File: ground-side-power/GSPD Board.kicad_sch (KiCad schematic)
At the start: 37 parts, among them J2 Battery Terminals, J4 Battery Terminals, J6 To SP2T, J7 From SP3T, J8 To On SW, J9 From Off SW, K1 AZ2150-1A-12DEF, U1 K7805-3AR3, U2 URB2424LD-20WR3

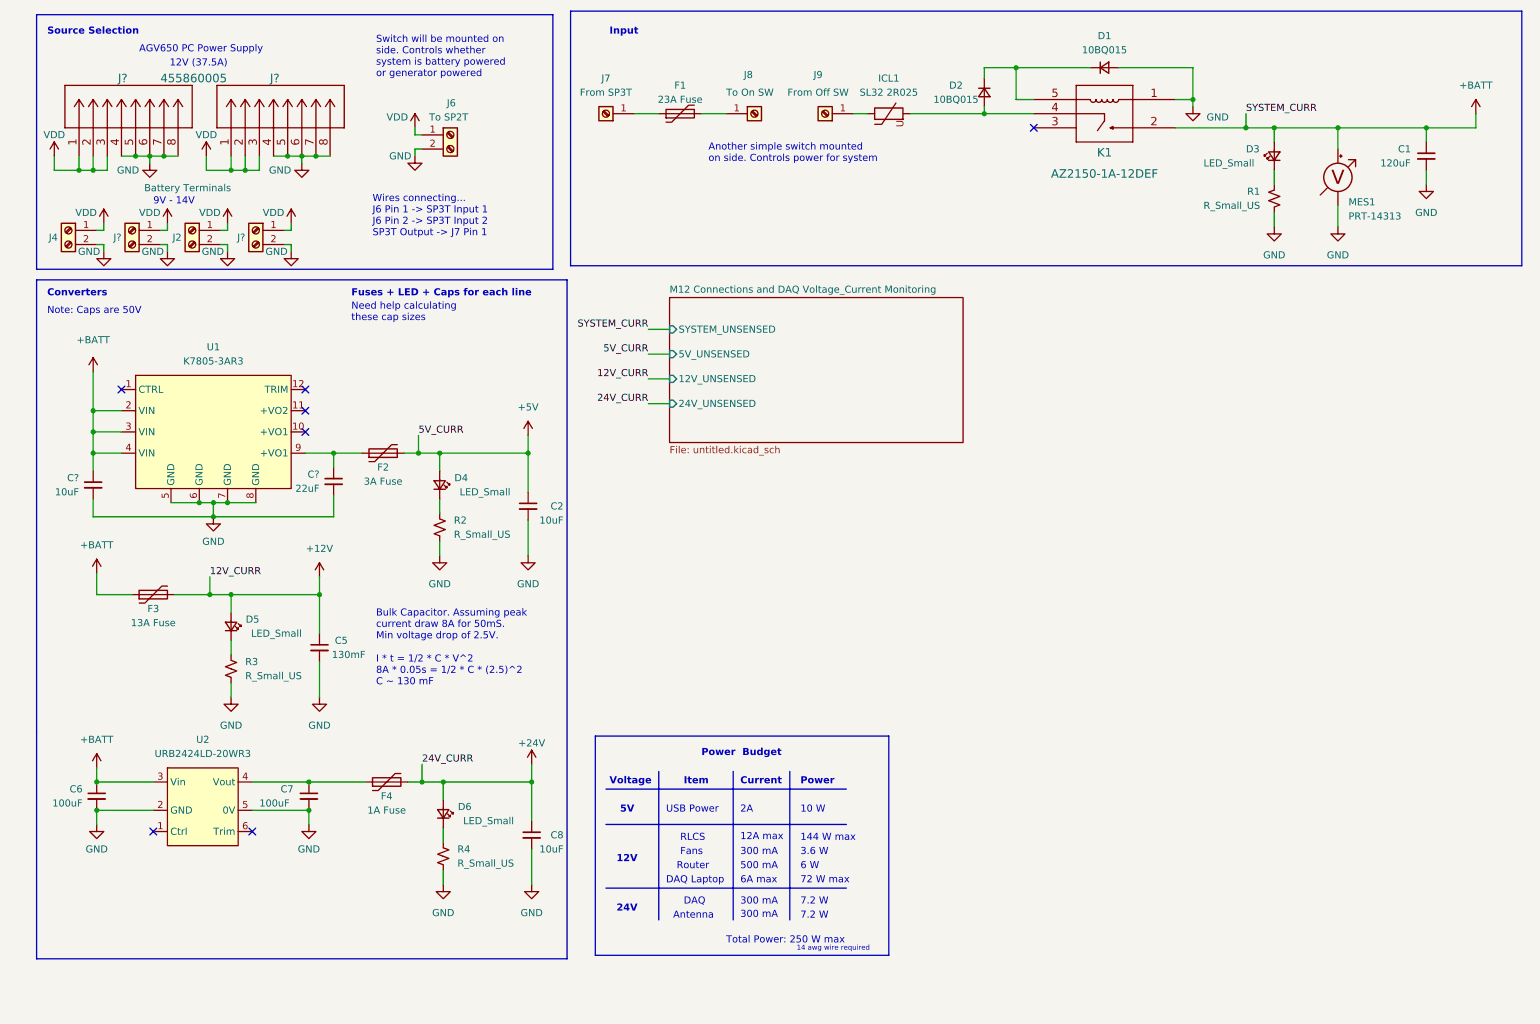
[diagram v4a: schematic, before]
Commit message: Changes to Shunt Current Sensors
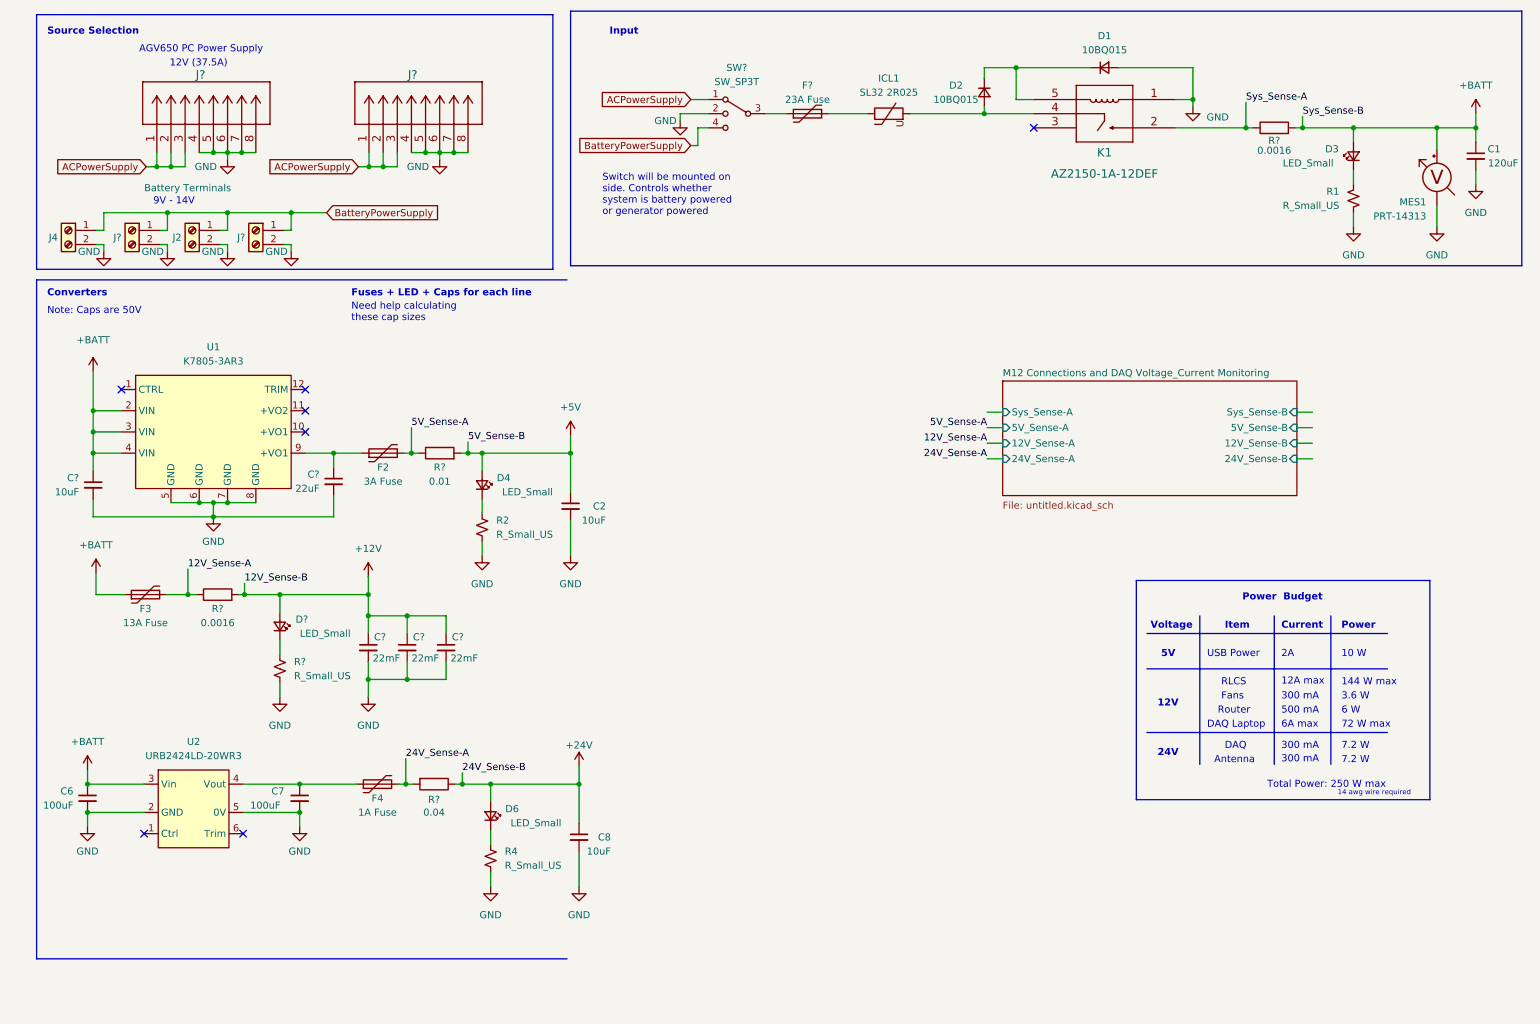
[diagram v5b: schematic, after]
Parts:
- removed C5: 130mF, symbol Device:C_Small
- removed D5: LED_Small, symbol Device:LED_Small
- removed F1: 23A Fuse, symbol Device:Polyfuse
- removed J6: To SP2T, symbol Connector:Screw_Terminal_01x02
- removed J7: From SP3T, symbol Connector:Screw_Terminal_01x01
- removed J8: To On SW, symbol Connector:Screw_Terminal_01x01
- removed J9: From Off SW, symbol Connector:Screw_Terminal_01x01
- removed J? (x2): 455860005, CON_455860005_MOL, symbol GSP:455860005
- removed R3: R_Small_US, symbol Device:R_Small_US
- added C? (x3): 22mF, symbol Device:C_Small
- added D?: LED_Small, symbol Device:LED_Small
- added F?: 23A Fuse, symbol Device:Polyfuse
- added J? (x2): 455860005, CON_455860005_MOL, symbol GSP:455860005
- added R? (x2): 0.0016, Resistor_SMD:R_1206_3216Metric_Pad1.42x1.75mm_HandSolder, symbol Device:R
- added R?: 0.01, Resistor_SMD:R_1206_3216Metric_Pad1.42x1.75mm_HandSolder, symbol Device:R
- added R?: 0.04, Resistor_SMD:R_1206_3216Metric_Pad1.42x1.75mm_HandSolder, symbol Device:R
- added R?: R_Small_US, symbol Device:R_Small_US
- added SW?: SW_SP3T, symbol Switch:SW_SP3T
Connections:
- net +12V: now also C?.1, C?.1, C?.1, D?.2 (A), R?.2; no longer F3.2
- net +24V: now also R?.1; no longer F4.2
- net +5V: now also R?.2; no longer F2.2
- net +BATT: now also R?.2; no longer K1.2
- net GND: now also C?.2, C?.2, C?.2, J?.4, J?.4, J?.5, J?.5, J?.6, J?.6, J?.7, J?.7, J?.8, J?.8, R?.1, SW?.2
- net at ICL1.1: now also F?.2
- net VDD renamed BatteryPowerSupply
- net BatteryPowerSupply: now also SW?.4
- new net: D?.1 (K), R?.2
- new net: F?.1, SW?.3
- new net 12V_Sense-A: F3.2, R?.1
- new net 24V_Sense-A: F4.2, R?.2
- new net 5V_Sense-A: F2.2, R?.1
- new net ACPowerSupply: J?.1, J?.1, J?.2, J?.2, J?.3, J?.3, SW?.1
- new net Sys_Sense-A: K1.2, R?.1
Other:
- sheet M12 Connections and DAQ Voltage_Current Monitoring ports: added 12V_Sense-A, 12V_Sense-B, 24V_Sense-A, 24V_Sense-B, 5V_Sense-A, 5V_Sense-B, Sys_Sense-A, Sys_Sense-B; removed 12V_UNSENSED, 24V_UNSENSED, 5V_UNSENSED, SYSTEM_UNSENSED
- note removed: "Another simple switch mounted on side. Controls power for system"
- note removed: "Bulk Capacitor. Assuming peak current draw 8A for 50mS. Min voltage drop of 2.5V."
- note removed: "I * t = 1/2 * C * V^2 8A * 0.05s = 1/2 * C * (2.5)^2 C ~ 130 mF"
- note removed: "Wires connecting... J6 Pin 1 -> SP3T Input 1 J6 Pin 2 -> SP3T Input 2 SP3T Output -> J7 Pin 1"
- moved on the sheet: C1, C2, C6, C7, C8, D3, D4, D6, F3, F4, MES1, R1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

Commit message: Addressed remaining comments
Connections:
- net at U1.10 (+VO1): now also C?.1, F2.1, U1.11 (+VO2), U1.9 (+VO1)
- no-connect marks 7 -> 5
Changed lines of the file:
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@@
   (junction (at 27.94 96.52) (diameter 0) (color 0 0 0 0)
+  )
+  (junction (at 71.12 92.71) (diameter 0) (color 0 0 0 0)
   )
   (junction (at 115.189 155.956) (diameter 0) (color 0 0 0 0)
@@
   (no_connect (at 196.85 38.1))
   (no_connect (at 33.02 85.09))
-  (no_connect (at 66.04 92.71))
-  (no_connect (at 66.04 88.9))
   (no_connect (at 66.04 85.09))
   (wire (pts (xy 52.07 59.055) (xy 52.07 60.325))
@@
     (stroke (width 0) (type default) (color 0 0 0 0))
   )
+  (polyline (pts (xy 125.73 187.325) (xy 111.76 187.325))
+    (stroke (width 0) (type default) (color 0 0 0 0))
+  )
   (wire (pts (xy 196.85 33.02) (xy 193.675 33.02))
     (stroke (width 0) (type default) (color 0 0 0 0))
@@
   )
   (wire (pts (xy 82.804 155.956) (xy 84.074 155.956))
+    (stroke (width 0) (type default) (color 0 0 0 0))
+  )
+  (wire (pts (xy 71.12 92.71) (xy 71.12 96.52))
+    (stroke (width 0) (type default) (color 0 0 0 0))
+  )
+  (wire (pts (xy 71.12 88.9) (xy 71.12 92.71))
     (stroke (width 0) (type default) (color 0 0 0 0))
   )
@@
     (stroke (width 0) (type default) (color 0 0 0 0))
   )
+  (wire (pts (xy 66.04 88.9) (xy 71.12 88.9))
+    (stroke (width 0) (type default) (color 0 0 0 0))
+  )
   (wire (pts (xy 85.09 91.948) (xy 85.09 96.52))
     (stroke (width 0) (type default) (color 0 0 0 0))
@@
     (stroke (width 0) (type default) (color 0 0 0 0))
   )
+  (polyline (pts (xy 125.73 65.405) (xy 125.73 187.325))
+    (stroke (width 0) (type default) (color 0 0 0 0))
+  )
   (wire (pts (xy 49.53 107.95) (xy 71.12 107.95))
     (stroke (width 0) (type default) (color 0 0 0 0))
@@
     (stroke (width 0) (type default) (color 0 0 0 0))
   )
+  (wire (pts (xy 66.04 92.71) (xy 71.12 92.71))
+    (stroke (width 0) (type default) (color 0 0 0 0))
+  )
   (wire (pts (xy 135.255 33.02) (xy 138.43 33.02))
     (stroke (width 0) (type default) (color 0 0 0 0))
@@
   )
   (wire (pts (xy 52.07 42.545) (xy 54.61 42.545))
+    (stroke (width 0) (type default) (color 0 0 0 0))
+  )
+  (polyline (pts (xy 113.03 65.405) (xy 125.73 65.405))
     (stroke (width 0) (type default) (color 0 0 0 0))
   )
@@
     (effects (font (size 1.27 1.27)) (justify left bottom))
   )
+  (label "12V_Sense-B" (at 246.888 94.742 0)
+    (effects (font (size 1.27 1.27)) (justify left bottom))
+  )
   (label "5V_Sense-B" (at 95.25 94.488 0)
     (effects (font (size 1.27 1.27)) (justify left bottom))
   )
+  (label "5V_Sense-B" (at 246.888 91.948 0)
+    (effects (font (size 1.27 1.27)) (justify left bottom))
+  )
   (label "Sys_Sense-B" (at 245.11 36.068 0)
     (effects (font (size 1.27 1.27)) (justify left bottom))
   )
   (label "24V_Sense-B" (at 94.234 153.924 0)
+    (effects (font (size 1.27 1.27)) (justify left bottom))
+  )
+  (label "Sys_Sense-B" (at 246.888 89.154 0)
     (effects (font (size 1.27 1.27)) (justify left bottom))
   )
@@
   (label "24V_Sense-A" (at 188.468 97.536 180)
     (effects (font (size 1.27 1.27)) (justify right bottom))
+  )
+  (label "Sys_Sense-A" (at 188.468 89.154 180)
+    (effects (font (size 1.27 1.27)) (justify right bottom))
+  )
+  (label "24V_Sense-B" (at 246.888 97.536 0)
+    (effects (font (size 1.27 1.27)) (justify left bottom))
   )
   (label "12V_Sense-A" (at 44.958 117.348 0)
@@
       (reference "#PWR021") (unit 1) (value "GND") (footprint "")
     )
-    (path "/bd13cf19-fc7f-4ae6-b380-53f95847a859/7c716f6f-a7b6-4de5-8703-4bb2af27e5da"
-      (reference "#PWR0102") (unit 1) (value "GND") (footprint "")
-    )
     (path "/bd13cf19-fc7f-4ae6-b380-53f95847a859/3d1ad647-60ef-4d81-9533-aae465ee1fbd"
       (reference "#PWR0103") (unit 1) (value "GND") (footprint "")
@@
       (reference "#PWR?") (unit 1) (value "GND") (footprint "")
     )
-    (path "/bd13cf19-fc7f-4ae6-b380-53f95847a859/d3e3be53-e07d-46f1-acc1-7560e255e047"
-      (reference "#PWR?") (unit 1) (value "+BATT") (footprint "")
-    )
     (path "/e27ca452-72d4-4c03-bada-023c33b821b2"
       (reference "#PWR?") (unit 1) (value "GND") (footprint "")
@@
       (reference "R4") (unit 1) (value "R_Small_US") (footprint "")
     )
-    (path "/bd13cf19-fc7f-4ae6-b380-53f95847a859/faa65dae-46de-4a23-9bff-b6d93a610804"
-      (reference "R5") (unit 1) (value "1k") (footprint "")
-    )
-    (path "/bd13cf19-fc7f-4ae6-b380-53f95847a859/5d9502d0-9e9e-4657-8809-a6f377939046"
-      (reference "R6") (unit 1) (value "2.2K") (footprint "")
-    )
     (path "/bd13cf19-fc7f-4ae6-b380-53f95847a859/3247f0ec-ba00-4be0-a76c-5ea0662a0032"
-      (reference "R7") (unit 1) (value "1K") (footprint "")
+      (reference "R7") (unit 1) (value "47K") (footprint "")
     )
     (path "/bd13cf19-fc7f-4ae6-b380-53f95847a859/331c1417-464e-4bf0-bde2-686c8657b71a"
-      (reference "R8") (unit 1) (value "330") (footprint "")
+      (reference "R8") (unit 1) (value "100K") (footprint "")
     )
     (path "/bd13cf19-fc7f-4ae6-b380-53f95847a859/d14a7f67-2fc7-4415-b64b-a9c6ee3f8748"
-      (reference "R9") (unit 1) (value "1k") (footprint "")
+      (reference "R9") (unit 1) (value "220K") (footprint "")
     )
     (path "/bd13cf19-fc7f-4ae6-b380-53f95847a859/fe4a6ae5-ac4c-4631-8c09-3b37c766b6c8"
-      (reference "R10") (unit 1) (value "2.2K") (footprint "")
+      (reference "R10") (unit 1) (value "100K") (footprint "")
     )
     (path "/bd13cf19-fc7f-4ae6-b380-53f95847a859/7d819bec-a493-4a15-a476-05085c9e7dbf"
-      (reference "R11") (unit 1) (value "1K") (footprint "")
+      (reference "R11") (unit 1) (value "660K") (footprint "")
     )
     (path "/bd13cf19-fc7f-4ae6-b380-53f95847a859/061830ce-cfdb-49f5-bab7-8c3e807e77eb"
-      (reference "R12") (unit 1) (value "6.6K") (footprint "")
+      (reference "R12") (unit 1) (value "100K") (footprint "")
     )
     (path "/019ff75b-9c7e-4961-b0ed-a5eed99de3dd"

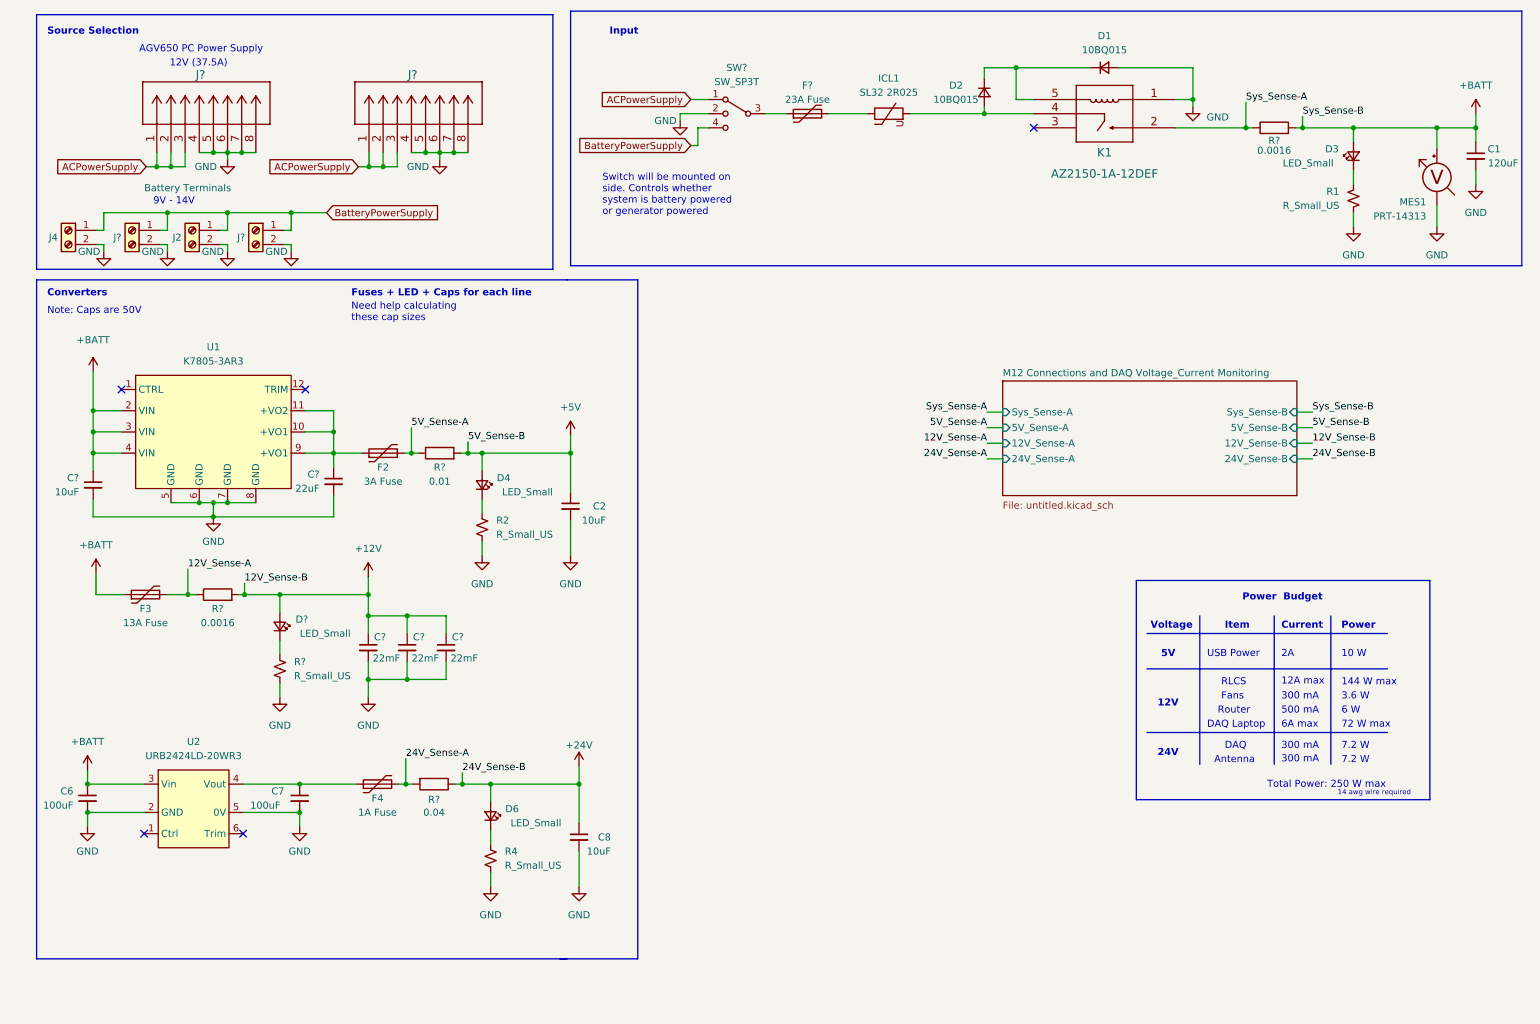
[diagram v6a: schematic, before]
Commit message: Changed PSU
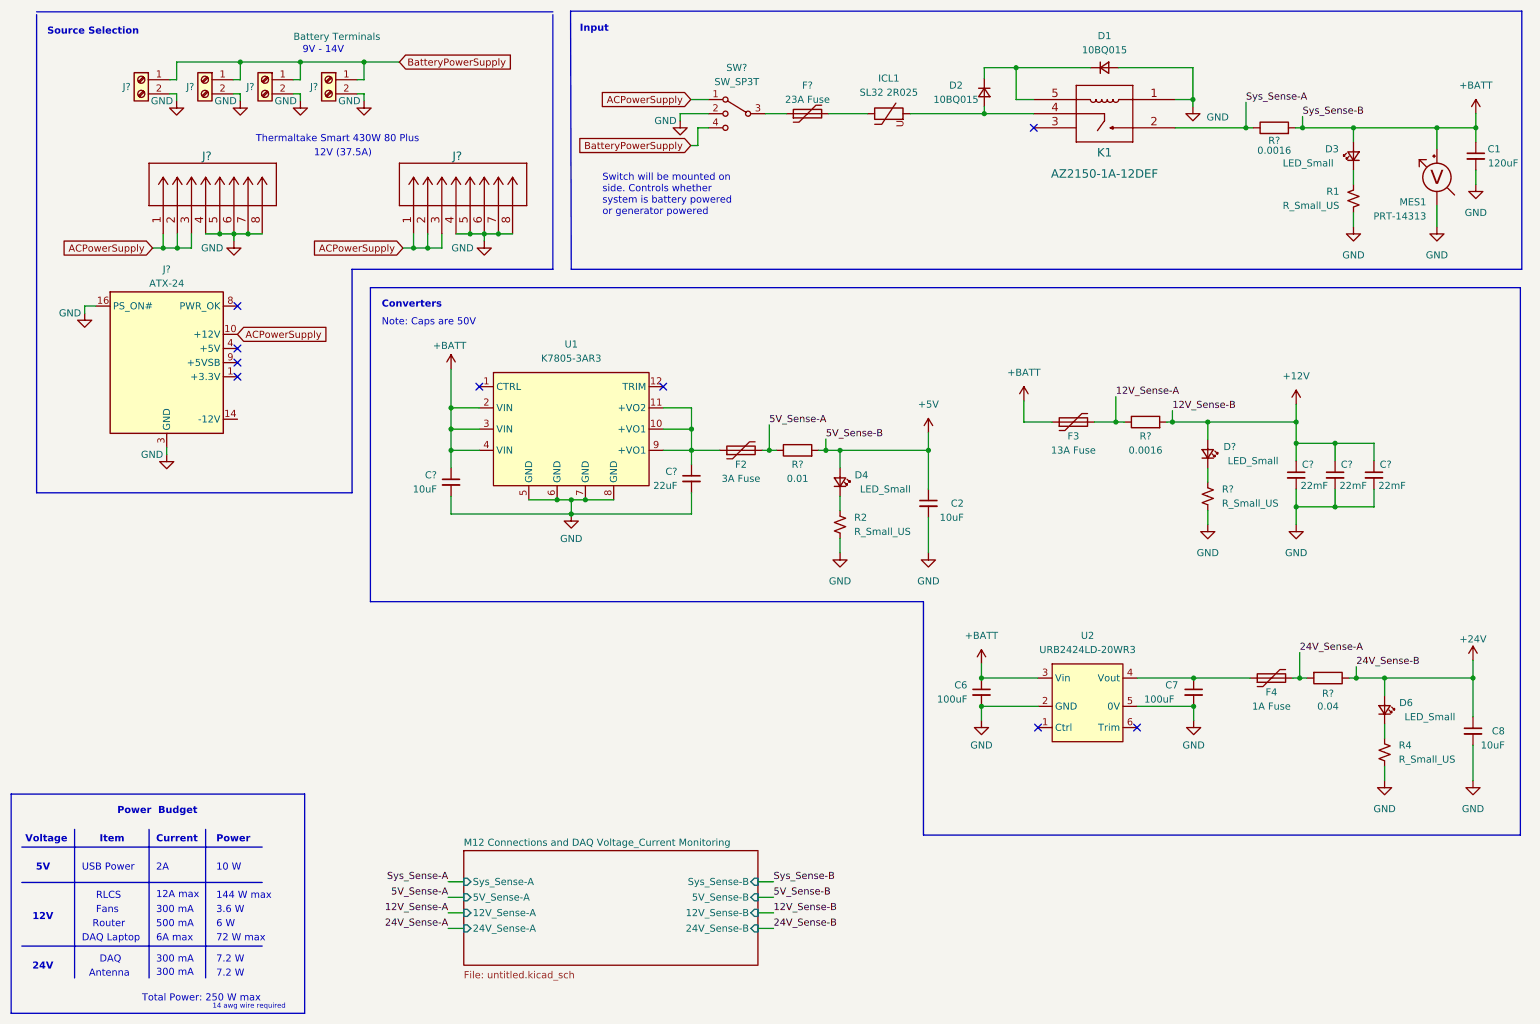
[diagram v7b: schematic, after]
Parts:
- removed J2, J4, J? (x2): Battery Terminals, symbol Connector:Screw_Terminal_01x02
- removed J? (x2): 455860005, CON_455860005_MOL, symbol GSP:455860005
- added J? (x4): Battery Terminals, symbol Connector:Screw_Terminal_01x02
- added J? (x2): 455860005, CON_455860005_MOL, symbol GSP:455860005
- added J?: ATX-24, symbol Connector:ATX-24
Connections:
- net ACPowerSupply: now also J?.1, J?.1, J?.10 (+12V), J?.11 (+12V), J?.2, J?.2, J?.3, J?.3
- net BatteryPowerSupply: now also J?.1 (Pin_1), J?.1 (Pin_1), J?.1 (Pin_1), J?.1 (Pin_1)
- net GND: now also J?.15 (GND), J?.16 (PS_ON#), J?.17 (GND), J?.18 (GND), J?.19 (GND), J?.2 (Pin_2), J?.2 (Pin_2), J?.2 (Pin_2), J?.2 (Pin_2), J?.24 (GND), J?.3 (GND), J?.4, J?.4, J?.5, J?.5, J?.5 (GND), J?.6, J?.6, J?.7, J?.7, J?.7 (GND), J?.8, J?.8
- new net: J?.1 (+3.3V), J?.12 (+3.3V), J?.13 (+3.3V), J?.2 (+3.3V)
- new net: J?.21 (+5V), J?.22 (+5V), J?.23 (+5V), J?.4 (+5V), J?.6 (+5V)
- no-connect marks 5 -> 9
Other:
- note added: "Thermaltake Smart 430W 80 Plus"
- note removed: "AGV650 PC Power Supply"
- note removed: "Fuses + LED + Caps for each line"
- note removed: "Need help calculating these cap sizes"
- moved on the sheet: C2, C6, C7, C8, C?, D4, D6, D?, F2, F3, F4, R2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
